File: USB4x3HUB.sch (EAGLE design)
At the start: 114 parts, among them IC1 TUSB2036, IC10 SN74LVC1G139DCUR, IC2 FSUSB74MPX, IC6 3.3V, IC7 5V, IC8 5V, IC9 5V, Q1 OSC4_6.0M, SW1 RD, SW2 BL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

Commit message: replace IC6-9 *CAUTION: airwires remain*
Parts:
- IC6: device mylib:LDO4_3.3_SOT223 -> mylib:LDO4_3.3_DRJ
- IC7, IC8, IC9: device mylib:LDO4_5.0_SOT223 -> mylib:LDO4_5.0_DRJ
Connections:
- net 3.3V: now also C14.1; no longer IC6.OUT/EN/NC
- net 5V1: no longer IC7.OUT/EN/NC
- net 5V2: no longer IC8.OUT/EN/NC
- net 5V3: no longer IC9.OUT/EN/NC
- net N$11: no longer C14.1
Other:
- moved on the sheet: C14
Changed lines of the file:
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@@
 <part name="C13" library="mylib" deviceset="C_SMD_*" device="_1005" technology="0.1U"/>
 <part name="SUPPLY17" library="mylib" deviceset="GND" device=""/>
-<part name="C14" library="mylib" deviceset="C_SMD_*" device="_2012" technology="4.7U"/>
 <part name="C15" library="mylib" deviceset="C_SMD_*" device="_2012" technology="4.7U"/>
 <part name="C16" library="mylib" deviceset="C_SMD_*" device="_2012" technology="4.7U"/>
@@
 <part name="R36" library="mylib" deviceset="R_US_*" device="_1005" technology="10K"/>
 <part name="R37" library="mylib" deviceset="R_US_*" device="_1005" technology="10K"/>
-<part name="IC6" library="mylib" deviceset="LDO4_*" device="_SOT223" technology="3.3" value="3.3V"/>
-<part name="IC7" library="mylib" deviceset="LDO4_*" device="_SOT223" technology="5.0" value="5V"/>
-<part name="IC8" library="mylib" deviceset="LDO4_*" device="_SOT223" technology="5.0" value="5V"/>
-<part name="IC9" library="mylib" deviceset="LDO4_*" device="_SOT223" technology="5.0" value="5V"/>
+<part name="IC6" library="mylib" deviceset="LDO4_*" device="_DRJ" technology="3.3" value="3.3V"/>
+<part name="IC7" library="mylib" deviceset="LDO4_*" device="_DRJ" technology="5.0" value="5V"/>
+<part name="IC8" library="mylib" deviceset="LDO4_*" device="_DRJ" technology="5.0" value="5V"/>
+<part name="IC9" library="mylib" deviceset="LDO4_*" device="_DRJ" technology="5.0" value="5V"/>
 <part name="R38" library="mylib" deviceset="R_US_*" device="_1005" technology="10K"/>
 <part name="TP100" library="mylib" deviceset="TESTPAD" device="_F"/>
@@
 <part name="R46" library="mylib" deviceset="R_US_*" device="_1005" technology="10K"/>
 <part name="R47" library="mylib" deviceset="R_US_*" device="_1005" technology="10K"/>
+<part name="C14" library="mylib" deviceset="C_SMD_*" device="_2012" technology="4.7U"/>
 </parts>
 <sheets>
@@
 <instance part="C13" gate="G$1" x="175.26" y="76.2" rot="R270"/>
 <instance part="SUPPLY17" gate="GND" x="182.88" y="76.2" rot="R90"/>
-<instance part="C14" gate="G$1" x="317.5" y="243.84"/>
 <instance part="C15" gate="G$1" x="322.58" y="215.9"/>
 <instance part="C16" gate="G$1" x="327.66" y="190.5"/>
@@
 <instance part="R46" gate="G$1" x="261.62" y="152.4"/>
 <instance part="R47" gate="G$1" x="299.72" y="139.7"/>
+<instance part="C14" gate="G$1" x="58.42" y="218.44"/>
 </instances>
 <busses>
@@
 <wire x1="304.8" y1="246.38" x2="312.42" y2="246.38" width="0.1524" layer="91"/>
 <pinref part="C8" gate="G$1" pin="1"/>
-<wire x1="312.42" y1="246.38" x2="317.5" y2="246.38" width="0.1524" layer="91"/>
 <junction x="312.42" y="246.38"/>
-<pinref part="C14" gate="G$1" pin="1"/>
-<wire x1="317.5" y1="246.38" x2="353.06" y2="246.38" width="0.1524" layer="91"/>
-<junction x="317.5" y="246.38"/>
+<wire x1="312.42" y1="246.38" x2="353.06" y2="246.38" width="0.1524" layer="91"/>
 </segment>
 </net>
@@
 <wire x1="35.56" y1="213.36" x2="35.56" y2="215.9" width="0.1524" layer="91"/>
 <pinref part="IC6" gate="G$1" pin="ADJ"/>
+<pinref part="C14" gate="G$1" pin="2"/>
+<wire x1="58.42" y1="215.9" x2="58.42" y2="210.82" width="0.1524" layer="91"/>
+<wire x1="58.42" y1="210.82" x2="48.26" y2="210.82" width="0.1524" layer="91"/>
+<wire x1="48.26" y1="210.82" x2="48.26" y2="213.36" width="0.1524" layer="91"/>
+<junction x="48.26" y="213.36"/>
 </segment>
 <segment>
@@
 <pinref part="IC3" gate="G$1" pin="GND"/>
 <pinref part="SUPPLY11" gate="GND" pin="GND"/>
-<wire x1="320.04" y1="241.3" x2="317.5" y2="241.3" width="0.1524" layer="91"/>
 <pinref part="C8" gate="G$1" pin="2"/>
-<wire x1="317.5" y1="241.3" x2="312.42" y2="241.3" width="0.1524" layer="91"/>
+<wire x1="320.04" y1="241.3" x2="312.42" y2="241.3" width="0.1524" layer="91"/>
 <wire x1="312.42" y1="241.3" x2="304.8" y2="241.3" width="0.1524" layer="91"/>
 <junction x="312.42" y="241.3"/>
-<pinref part="C14" gate="G$1" pin="2"/>
-<junction x="317.5" y="241.3"/>
 </segment>
 <segment>
@@
 <segment>
 <wire x1="55.88" y1="220.98" x2="58.42" y2="220.98" width="0.1524" layer="91"/>
+<label x="66.04" y="220.98" size="1.778" layer="95"/>
+<pinref part="IC6" gate="G$1" pin="OUT"/>
+<pinref part="C14" gate="G$1" pin="1"/>
 <wire x1="58.42" y1="220.98" x2="66.04" y2="220.98" width="0.1524" layer="91"/>
 <junction x="58.42" y="220.98"/>
-<label x="66.04" y="220.98" size="1.778" layer="95"/>
-<wire x1="48.26" y1="226.06" x2="58.42" y2="226.06" width="0.1524" layer="91"/>
-<wire x1="58.42" y1="226.06" x2="58.42" y2="220.98" width="0.1524" layer="91"/>
-<pinref part="IC6" gate="G$1" pin="OUT"/>
-<pinref part="IC6" gate="G$1" pin="OUT/EN/NC"/>
 </segment>
 <segment>
@@
 <net name="5V1" class="0">
 <segment>
-<wire x1="231.14" y1="246.38" x2="279.4" y2="246.38" width="0.1524" layer="91"/>
+<wire x1="228.6" y1="246.38" x2="279.4" y2="246.38" width="0.1524" layer="91"/>
 <pinref part="IC3" gate="G$1" pin="VIN"/>
 <label x="233.68" y="246.38" size="1.778" layer="95"/>
@@
 <wire x1="279.4" y1="246.38" x2="284.48" y2="246.38" width="0.1524" layer="91"/>
 <junction x="279.4" y="246.38"/>
-<wire x1="228.6" y1="246.38" x2="231.14" y2="246.38" width="0.1524" layer="91"/>
-<wire x1="220.98" y1="251.46" x2="231.14" y2="251.46" width="0.1524" layer="91"/>
-<wire x1="231.14" y1="251.46" x2="231.14" y2="246.38" width="0.1524" layer="91"/>
-<junction x="231.14" y="246.38"/>
 <pinref part="IC7" gate="G$1" pin="OUT"/>
-<pinref part="IC7" gate="G$1" pin="OUT/EN/NC"/>
 </segment>
 </net>
@@
 <label x="259.08" y="218.44" size="1.778" layer="95"/>
 <pinref part="C6" gate="G$1" pin="1"/>
-<wire x1="256.54" y1="218.44" x2="284.48" y2="218.44" width="0.1524" layer="91"/>
+<wire x1="254" y1="218.44" x2="284.48" y2="218.44" width="0.1524" layer="91"/>
 <wire x1="284.48" y1="218.44" x2="289.56" y2="218.44" width="0.1524" layer="91"/>
 <junction x="284.48" y="218.44"/>
-<wire x1="254" y1="218.44" x2="256.54" y2="218.44" width="0.1524" layer="91"/>
-<wire x1="246.38" y1="223.52" x2="256.54" y2="223.52" width="0.1524" layer="91"/>
-<wire x1="256.54" y1="223.52" x2="256.54" y2="218.44" width="0.1524" layer="91"/>
-<junction x="256.54" y="218.44"/>
 <pinref part="IC8" gate="G$1" pin="OUT"/>
-<pinref part="IC8" gate="G$1" pin="OUT/EN/NC"/>
 </segment>
 </net>
@@
 <wire x1="289.56" y1="193.04" x2="294.64" y2="193.04" width="0.1524" layer="91"/>
 <junction x="289.56" y="193.04"/>
-<wire x1="281.94" y1="193.04" x2="289.56" y2="193.04" width="0.1524" layer="91"/>
-<wire x1="279.4" y1="193.04" x2="281.94" y2="193.04" width="0.1524" layer="91"/>
-<wire x1="271.78" y1="198.12" x2="281.94" y2="198.12" width="0.1524" layer="91"/>
-<wire x1="281.94" y1="198.12" x2="281.94" y2="193.04" width="0.1524" layer="91"/>
-<junction x="281.94" y="193.04"/>
+<wire x1="279.4" y1="193.04" x2="289.56" y2="193.04" width="0.1524" layer="91"/>
 <pinref part="IC9" gate="G$1" pin="OUT"/>
-<pinref part="IC9" gate="G$1" pin="OUT/EN/NC"/>
-</segment>
-</net>
+</segment>
+</net>

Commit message: C8-11 replaced by OS-CON 16V/100uF; PCB width shrinked 10mm(and necessary moves)
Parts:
- removed C15, C16: (no value), mylib:C_SMD_4.7U_2012
- removed PCB1: PCB_DP_SQUARE-7X7, dp_pcb:PCB_DP_SQUARE-7X7
- C10, C8, C9: value (none) -> C_DENKAI_100U_2.5P6.3_C6; device mylib:C_SMD_4.7U_2012 -> mylib:C_DENKAI_100U_2.5P6.3_C6
- C11: value C_DENKAI_100U_2.5P5 -> C_DENKAI_100U_2.5P6.3_C6; device mylib:C_DENKAI_100U_2.5P5 -> mylib:C_DENKAI_100U_2.5P6.3_C6
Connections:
- net GND: now also C10.-, C8.-, C9.-, CON5.GND, CON6.GND, CON7.GND; no longer C10.2, C15.2, C16.2, C8.2, C9.2
- net N$11: now also C8.+; no longer C8.1
- net N$12: now also C9.+; no longer C15.1, C9.1
- net N$13: now also C10.+; no longer C10.1, C16.1
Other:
- moved on the sheet: CON5, CON6, CON7

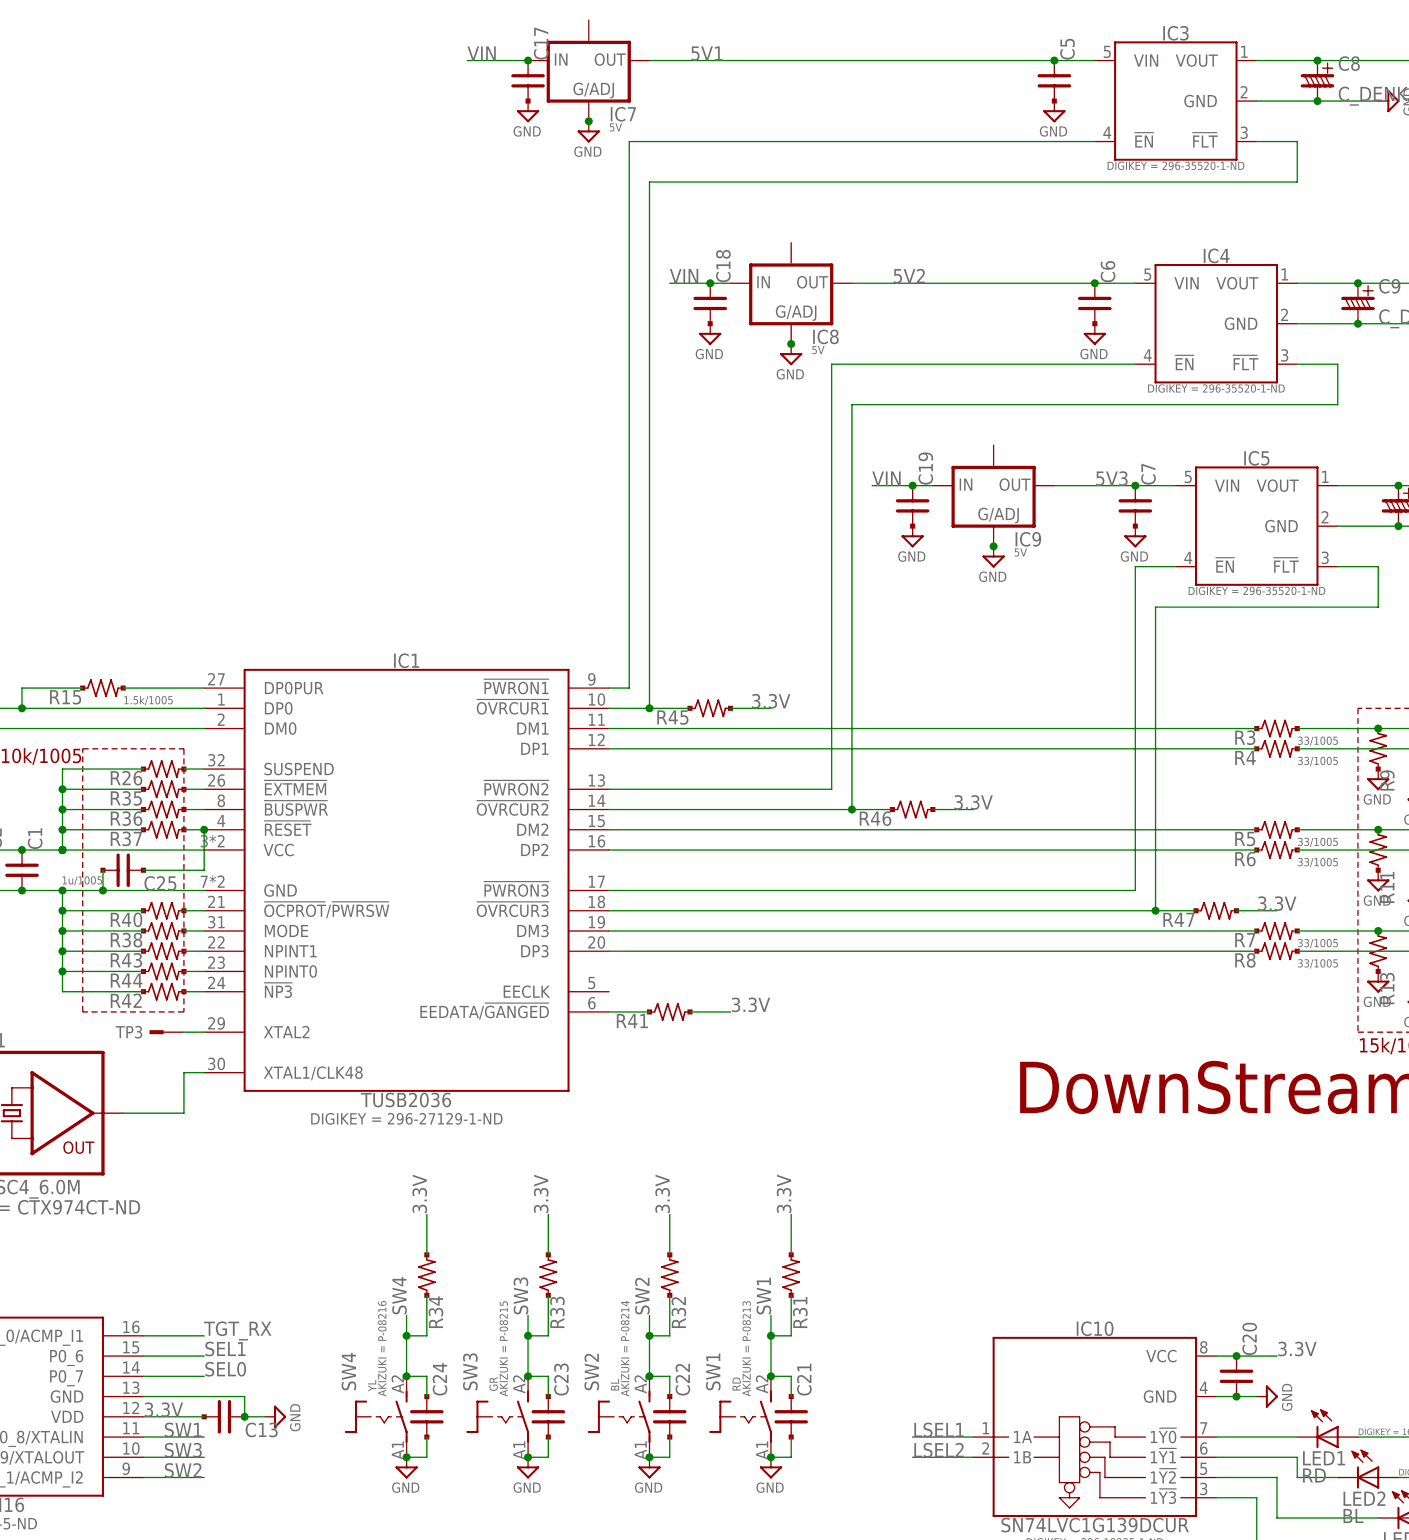
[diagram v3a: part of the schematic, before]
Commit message: Capacitors renumbered
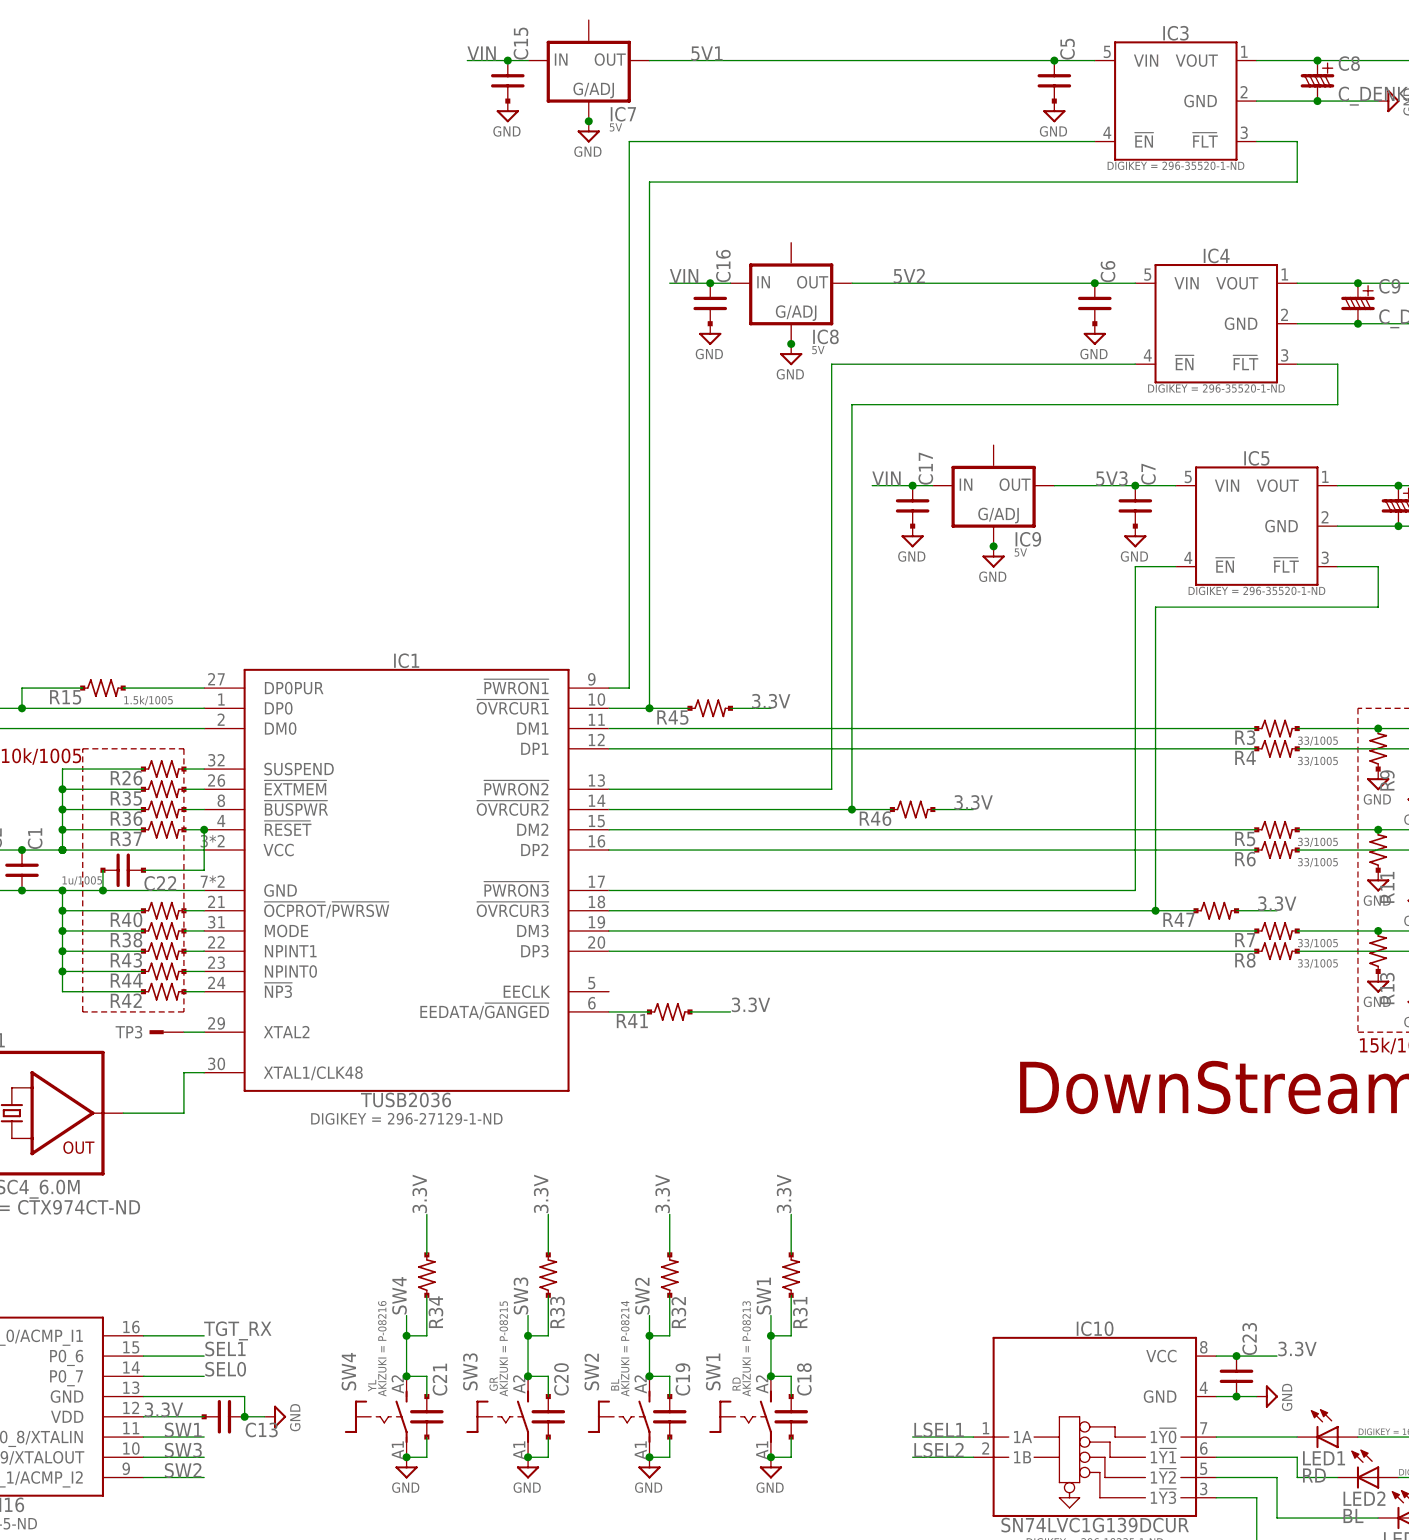
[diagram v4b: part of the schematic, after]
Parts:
- removed C24: (no value), mylib:C_SMD_0.1U_1005
- removed C25: 1u/1005, mylib:C_SMD_1.0U_1005
- added C15, C16: (no value), mylib:C_SMD_4.7U_2012
- C18, C19: device mylib:C_SMD_4.7U_2012 -> mylib:C_SMD_0.1U_1005
- C22: value (none) -> 1u/1005; device mylib:C_SMD_0.1U_1005 -> mylib:C_SMD_1.0U_1005
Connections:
- net 3.3V: now also C23.1; no longer C20.1
- net GND: now also C15.2, C16.2; no longer C24.2, C25.2
- net N$62: now also C22.1; no longer C25.1
- net SW1: now also C18.1; no longer C21.1
- net SW2: now also C19.1; no longer C22.1
- net SW3: now also C20.1; no longer C23.1
- net SW4: now also C21.1; no longer C24.1
- net VIN: now also C15.1, C16.1; no longer C18.1, C19.1
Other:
- moved on the sheet: C17, C18, C19, C20, C21, C22, C23
